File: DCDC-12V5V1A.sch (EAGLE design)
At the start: 34 parts, among them U1 TPS63060DSCT

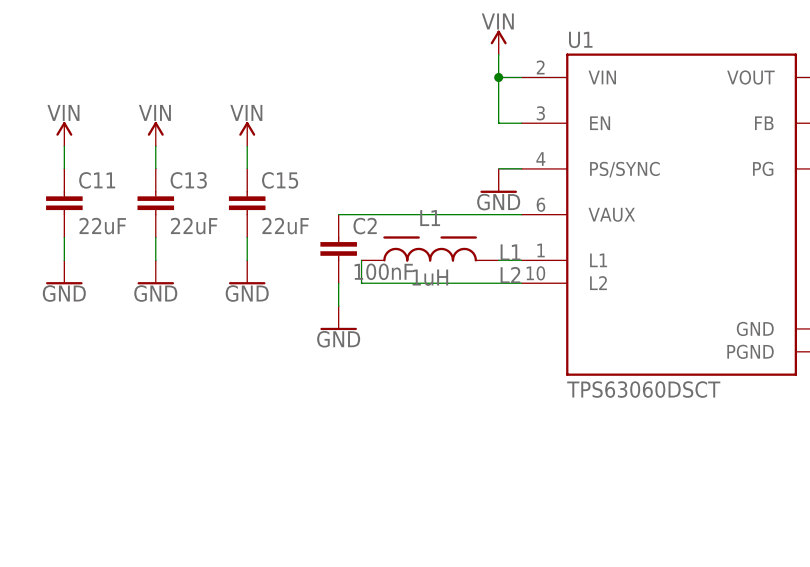
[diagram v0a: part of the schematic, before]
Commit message: Changed L1 inductor from 1uH to 1.5uH for higher output current stability. Generated PDF schematics. Updated BoM file.
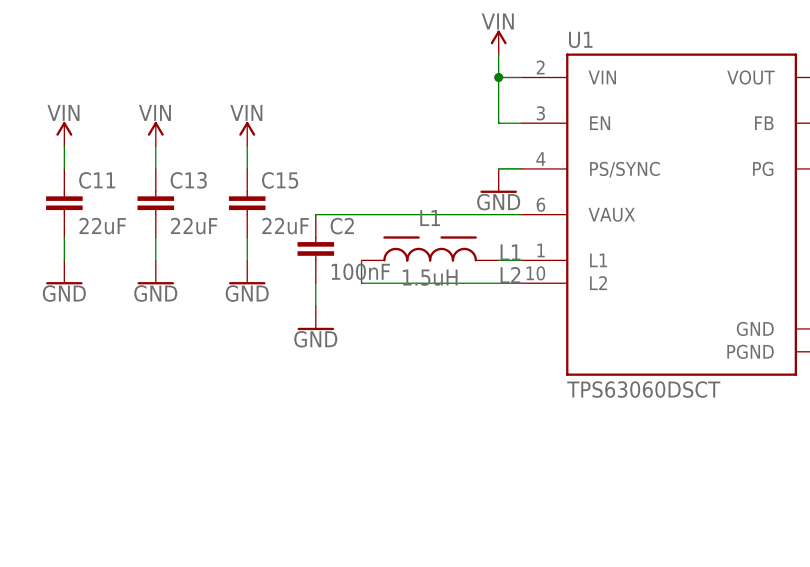
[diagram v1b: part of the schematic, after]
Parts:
- L1: value 1uH -> 1.5uH
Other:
- moved on the sheet: C2
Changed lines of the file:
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@@
 <part name="GND7" library="SparkFun-PowerSymbols" library_urn="urn:adsk.eagle:library:530" deviceset="GND" device=""/>
 <part name="C2" library="rcl" library_urn="urn:adsk.eagle:library:334" deviceset="C-EU" device="C0603K" package3d_urn="urn:adsk.eagle:package:23680/2" value="100nF"/>
-<part name="L1" library="Wurth_Power Magnetics_WE-LQS" library_urn="urn:adsk.eagle:library:14283646" deviceset="WE-LQS_4018" device="" package3d_urn="urn:adsk.eagle:package:13009659/3" technology="_74404042010" value="1uH"/>
+<part name="L1" library="Wurth_Power Magnetics_WE-LQS" library_urn="urn:adsk.eagle:library:14283646" deviceset="WE-LQS_4018" device="" package3d_urn="urn:adsk.eagle:package:13009659/3" technology="_74404042010" value="1.5uH"/>
 </parts>
 <sheets>
@@
 <attribute name="VALUE" x="137.16" y="127.254" size="1.778" layer="96" align="bottom-center"/>
 </instance>
-<instance part="GND6" gate="1" x="78.74" y="93.98" smashed="yes">
-<attribute name="VALUE" x="78.74" y="93.726" size="1.778" layer="96" align="top-center"/>
+<instance part="GND6" gate="1" x="76.2" y="93.98" smashed="yes">
+<attribute name="VALUE" x="76.2" y="93.726" size="1.778" layer="96" align="top-center"/>
 </instance>
 <instance part="R2" gate="G$1" x="142.24" y="111.76" smashed="yes">
@@
 <attribute name="VALUE" x="96.52" y="108.966" size="1.778" layer="96" align="top-center"/>
 </instance>
-<instance part="C2" gate="G$1" x="78.74" y="104.14" smashed="yes">
-<attribute name="NAME" x="80.264" y="104.521" size="1.778" layer="95"/>
-<attribute name="VALUE" x="80.264" y="99.441" size="1.778" layer="96"/>
+<instance part="C2" gate="G$1" x="76.2" y="104.14" smashed="yes">
+<attribute name="NAME" x="77.724" y="104.521" size="1.778" layer="95"/>
+<attribute name="VALUE" x="77.724" y="99.441" size="1.778" layer="96"/>
 </instance>
 <instance part="L1" gate="G$1" x="88.9" y="101.6" smashed="yes">
@@
 <segment>
 <pinref part="GND6" gate="1" pin="GND"/>
-<wire x1="78.74" y1="99.06" x2="78.74" y2="96.52" width="0.1524" layer="91"/>
+<wire x1="76.2" y1="99.06" x2="76.2" y2="96.52" width="0.1524" layer="91"/>
 <pinref part="C2" gate="G$1" pin="2"/>
 </segment>
@@
 <net name="VINA" class="0">
 <segment>
-<wire x1="99.06" y1="106.68" x2="78.74" y2="106.68" width="0.1524" layer="91"/>
+<wire x1="99.06" y1="106.68" x2="76.2" y2="106.68" width="0.1524" layer="91"/>
 <pinref part="U1" gate="G$1" pin="VAUX"/>
 <pinref part="C2" gate="G$1" pin="1"/>
